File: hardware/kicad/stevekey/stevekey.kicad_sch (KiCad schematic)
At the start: 15 parts

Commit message: Start board layout
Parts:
- removed U? (x5): CD4066BM, Package_SO:SO-14_3.9x8.65mm_P1.27mm, symbol Analog_Switch:CD4066BM
- added C1, C2: C_Small, Capacitor_THT:C_Disc_D5.0mm_W2.5mm_P5.00mm, symbol Device:C_Small
- added J1: ATMEL-ICE-10, stevekey:PinHeader_2x05_P1.27mm_Shrouded_Vertical_SMD_Handsolder, symbol stevekey:ATMEL-ICE-10
- added J2: Conn_01x04, Connector_PinHeader_2.54mm:PinHeader_1x04_P2.54mm_Vertical, symbol Connector_Generic:Conn_01x04
- added J3, J4, J5: Conn_01x02, Connector_PinHeader_2.54mm:PinHeader_1x02_P2.54mm_Vertical, symbol Connector_Generic:Conn_01x02
- added SW1: SW_SL, Button_Switch_Keyboard:SW_Cherry_MX_1.00u_PCB, symbol Switch:SW_Push
- added SW2: SW_CAPS, Button_Switch_Keyboard:SW_Cherry_MX_1.00u_PCB, symbol Switch:SW_Push
- added SW3: SW_4080, Button_Switch_Keyboard:SW_Cherry_MX_1.00u_PCB, symbol Switch:SW_Push
- added U1: CD4066BE, Package_DIP:DIP-14_W7.62mm, symbol Analog_Switch:CD4066BE
- D1, D2, D3: renamed from D?; footprint (none) -> LED_THT:LED_D5.0mm
- R1, R2, R3, R4, R5, R6: renamed from R?; footprint (none) -> Resistor_THT:R_Axial_DIN0204_L3.6mm_D1.6mm_P7.62mm_Horizontal
- gave numbers to parts that had none: 1
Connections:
- net 4080OUT: now also U1.6
- net CAPSOUT: now also U1.5
- net GND: now also C1.2, C2.2, J1.10 (GND), J1.2 (GND), SW1.1, SW2.1, SW3.1, U1.7 (V_{SS})
- net N4080KEY: now also SW3.2
- net NCAPSKEY: now also SW2.2
- net NSLKEY: now also SW1.2
- net SLOUT: now also U1.13
- net UPDI: now also J1.3 (UPDI/TDO)
- net VCC: now reaches R1.1, R2.1, R3.1, R4.1, R5.1, R6.1, U2.1 (VCC)
- net VCC: now also C1.1, C2.1, J1.4 (VTG), U1.14 (V_{DD})
- new net: J4.2 (Pin_2), U1.3
- new net: J4.1 (Pin_1), U1.4
- new net: J3.1 (Pin_1), U1.1
- new net: J3.2 (Pin_2), U1.2
- new net: J5.1 (Pin_1), U1.8
- new net: J5.2 (Pin_2), U1.9
- no-connect marks 1 -> 8

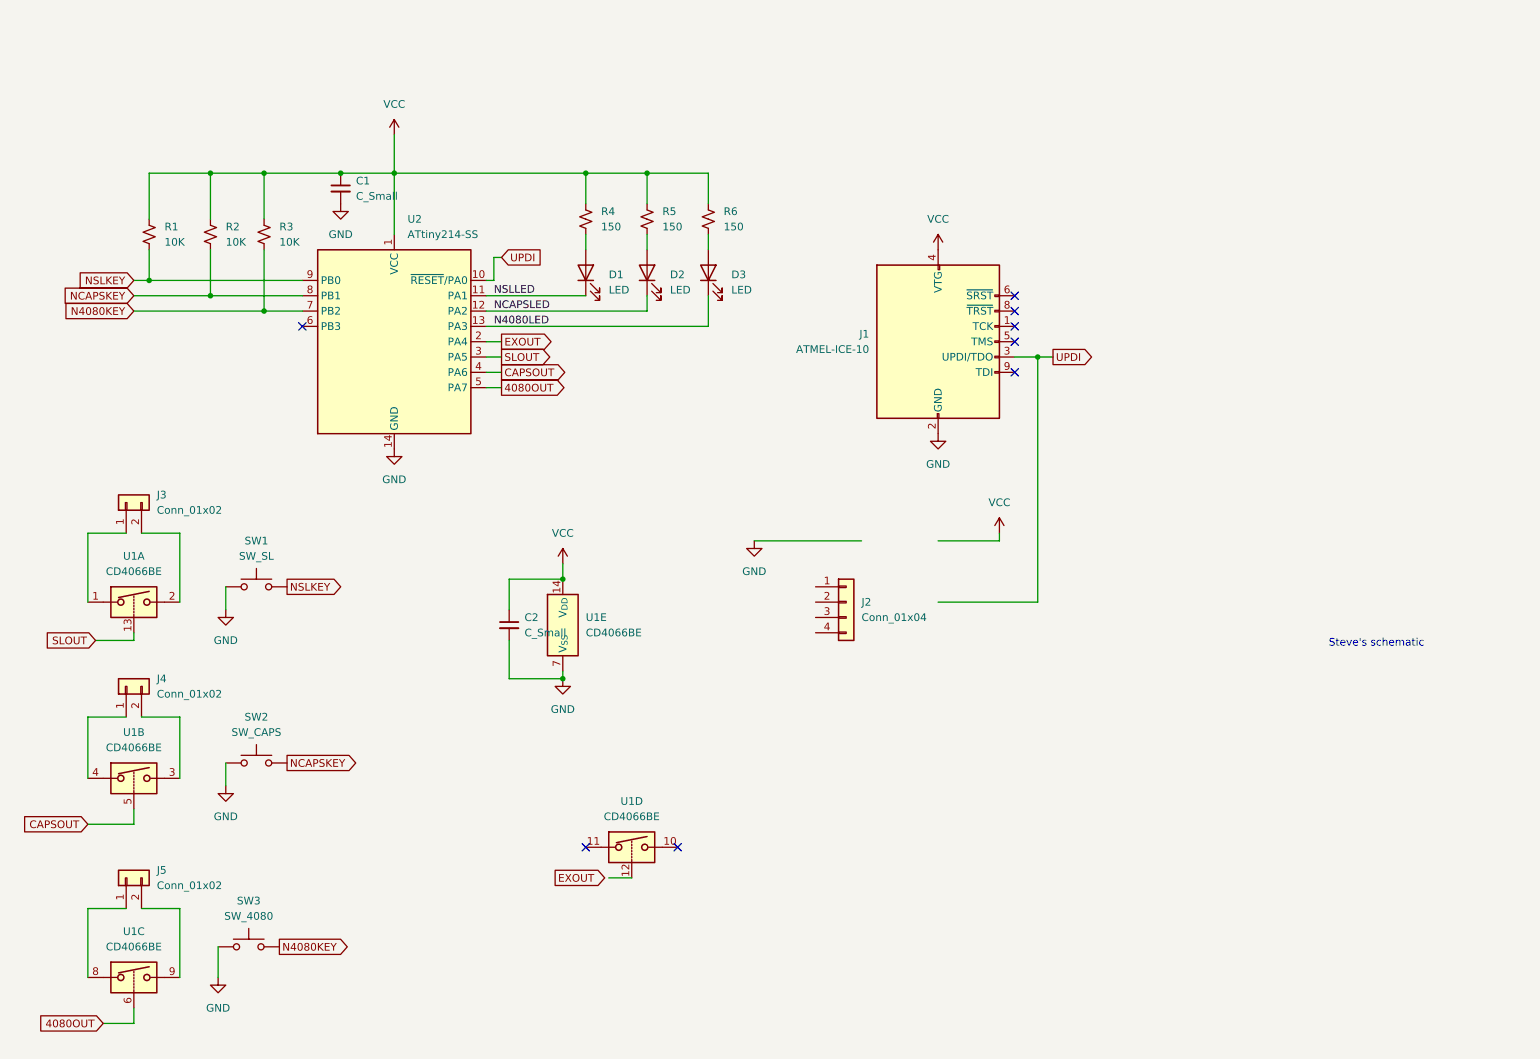
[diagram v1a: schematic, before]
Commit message: Initial routing is complete
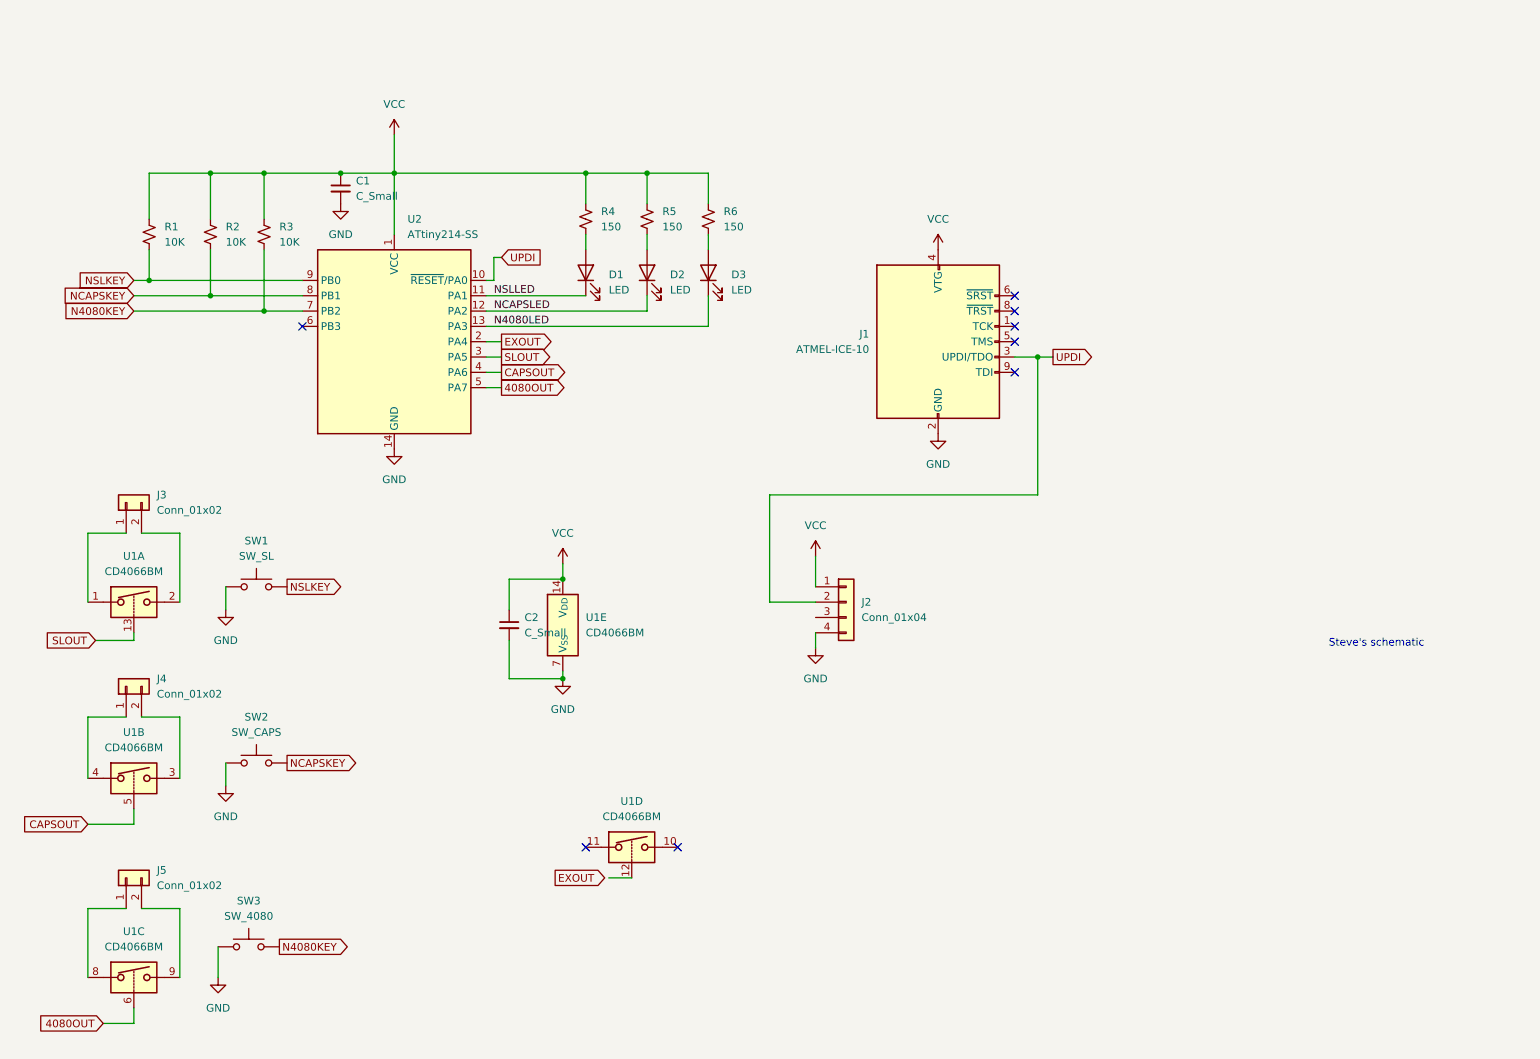
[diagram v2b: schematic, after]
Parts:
- removed U1: CD4066BE, Package_DIP:DIP-14_W7.62mm, symbol Analog_Switch:CD4066BE
- added U1: CD4066BM, Package_SO:SO-14_3.9x8.65mm_P1.27mm, symbol Analog_Switch:CD4066BM
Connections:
- net 4080OUT: now also U1.6
- net CAPSOUT: now also U1.5
- net GND: now also J2.4 (Pin_4), U1.7 (V_{SS})
- net SLOUT: now also U1.13
- net UPDI: now also J2.2 (Pin_2)
- net VCC: now also J2.1 (Pin_1), U1.14 (V_{DD})
- net at J4.2 (Pin_2): now also U1.3
- net at J4.1 (Pin_1): now also U1.4
- net at J3.1 (Pin_1): now also U1.1
- net at J3.2 (Pin_2): now also U1.2
- net at J5.1 (Pin_1): now also U1.8
- net at J5.2 (Pin_2): now also U1.9

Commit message: Add transistor to pull /RES down
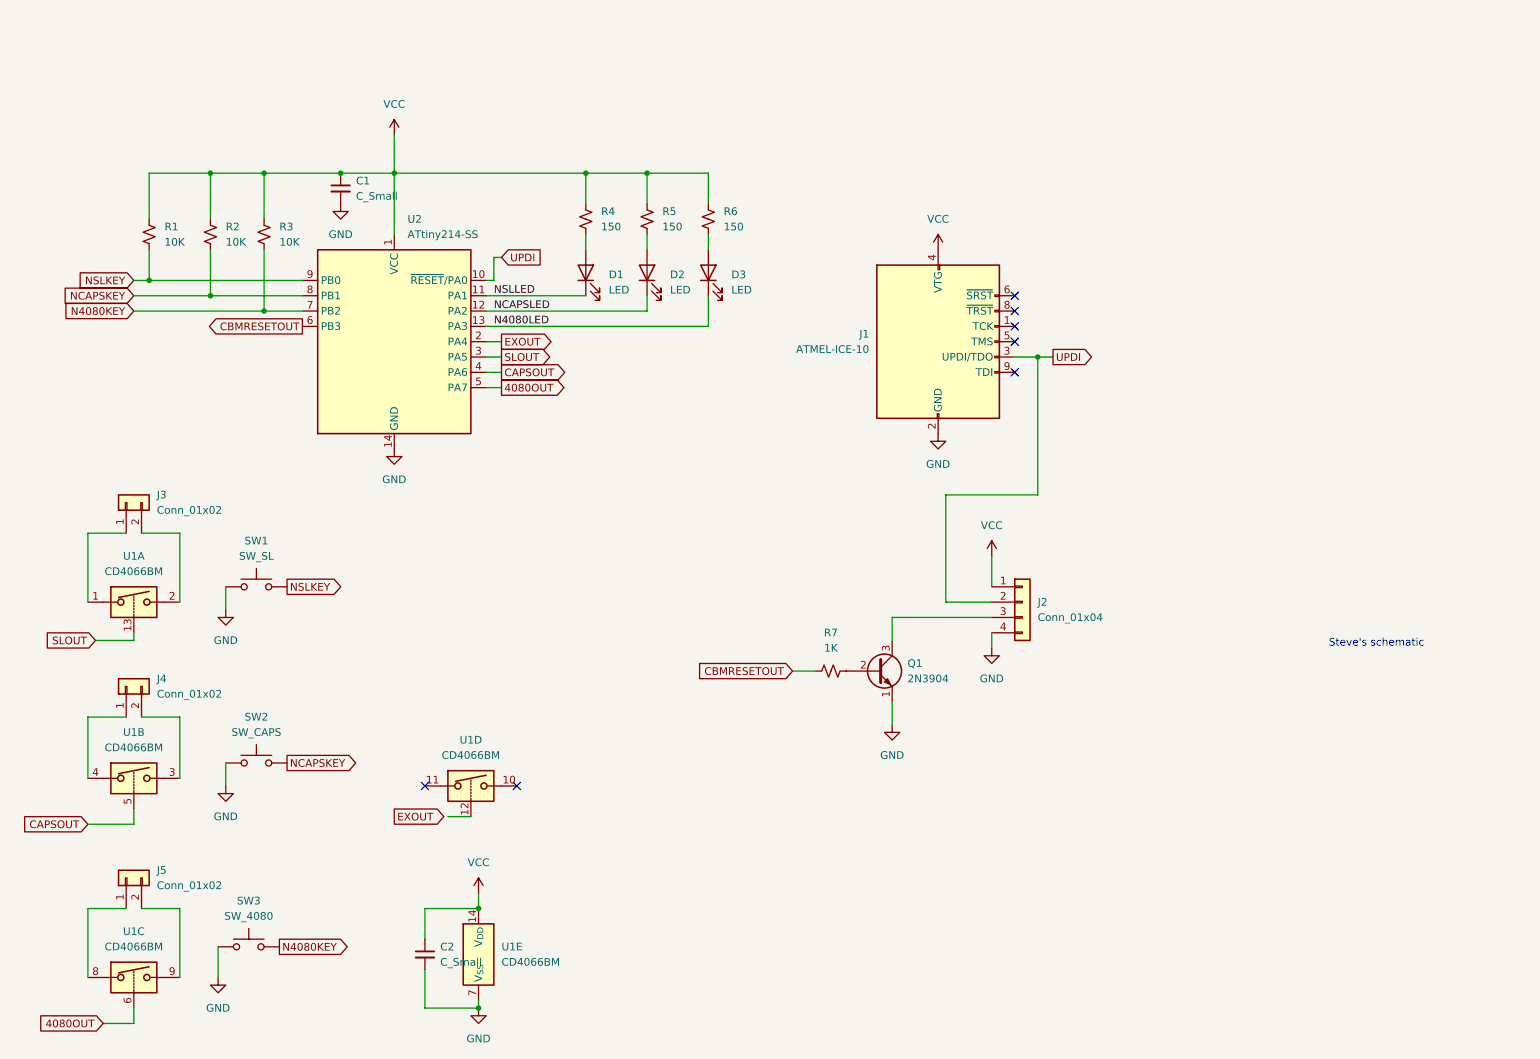
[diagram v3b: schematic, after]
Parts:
- added Q1: 2N3904, Package_TO_SOT_THT:TO-92_Inline, symbol Transistor_BJT:2N3904
- added R7: 1K, Resistor_THT:R_Axial_DIN0204_L3.6mm_D1.6mm_P7.62mm_Horizontal, symbol Device:R_Small_US
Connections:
- net GND: now also Q1.1 (E)
- net CBMRESETOUT: now reaches U2.6 (PB3)
- net CBMRESETOUT: now also R7.1
- net at J2.3 (Pin_3): now also Q1.3 (C)
- new net: Q1.2 (B), R7.2
- no-connect marks 8 -> 7
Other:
- moved on the sheet: C2, J2, U1D, U1E
